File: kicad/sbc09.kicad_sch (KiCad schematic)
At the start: 82 parts, among them J1 Conn_01x04_Male, J2 Conn_01x06_Male, J3 Conn_01x06_Male, J4 Conn_01x06_Male, J5 Conn_02x05_Odd_Even, J6 Conn_02x25_Odd_Even, J7 Conn_02x05_Odd_Even, Q1 2N7000, SW1 SW_Push, U1 74HCT245, U10 SST39SF040-DIP, U11 XR68C681CJ, U12 MAX232, U2 74HCT245, U3 74HCT245, U4 MC6809E, U5 74HCT32, U6 EPM7128SLC84, U7 71256SA15TPG, U8 AS6C4008-55PCN, U9 SST39SF040-DIP, X1 8MHz, X2 3.6864MHz

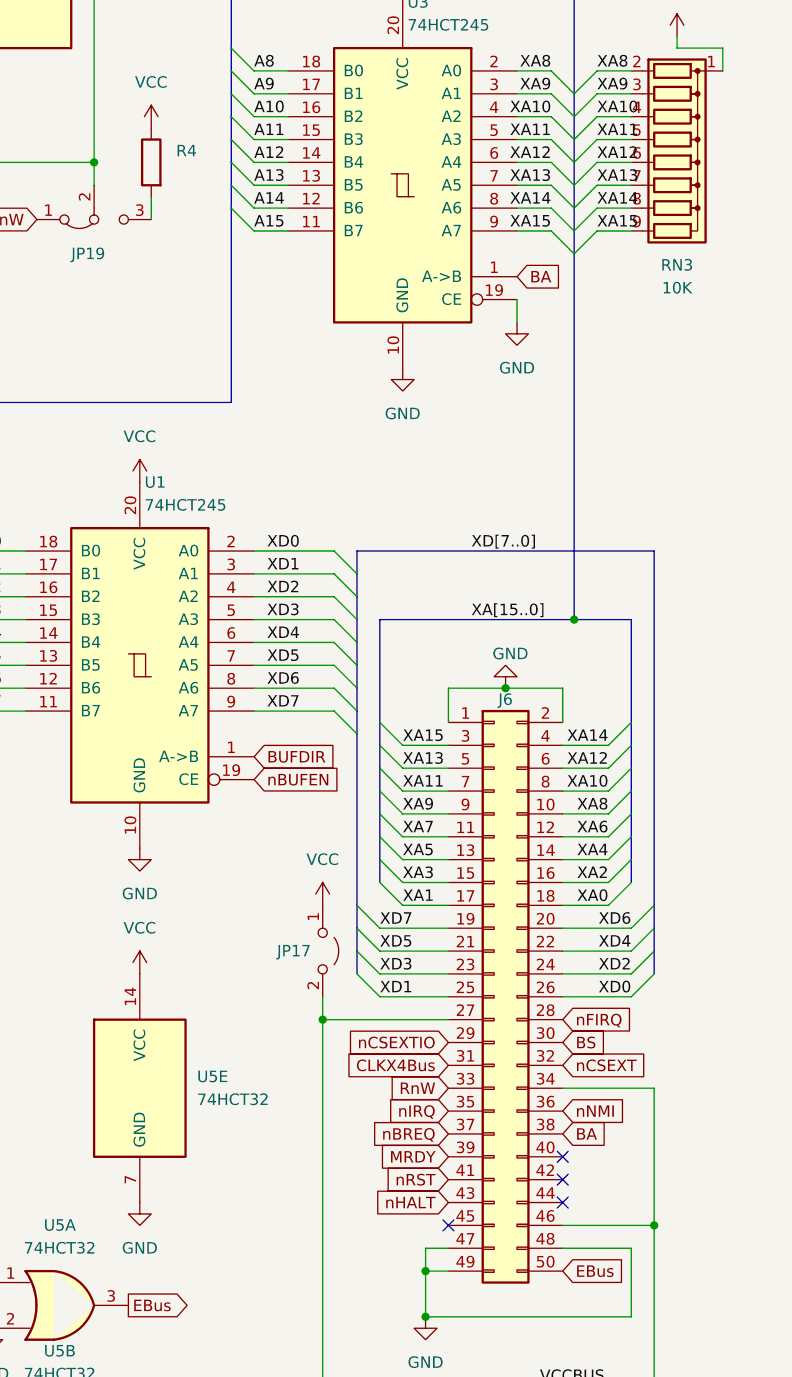
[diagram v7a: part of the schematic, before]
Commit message: KiCAD: Connect QA13/14/15 to spare pins on the backplane connector (review assignments)
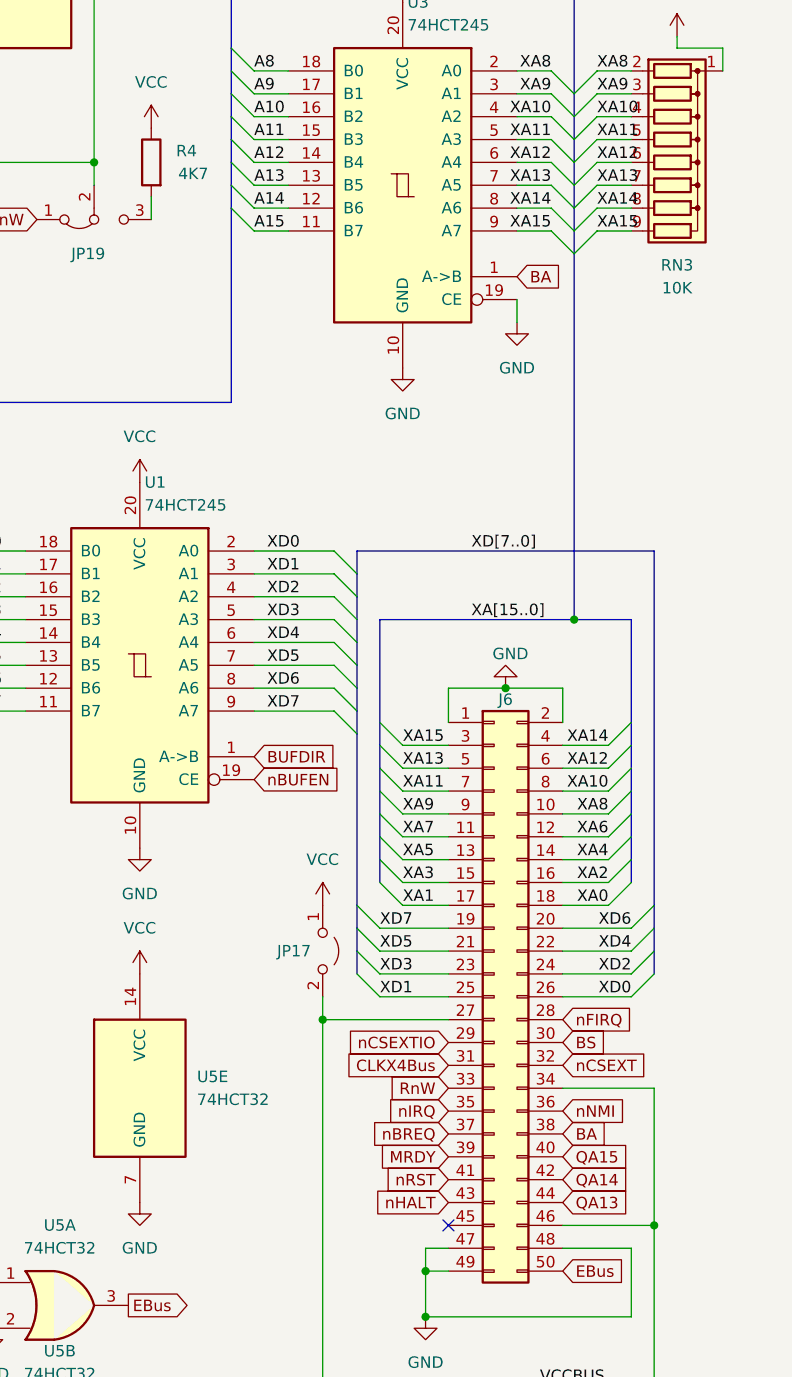
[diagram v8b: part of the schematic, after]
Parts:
- R4: value (none) -> 4K7
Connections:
- net QA13: now also J6.44 (Pin_44)
- net QA14: now also J6.42 (Pin_42)
- net QA15: now also J6.40 (Pin_40)
- no-connect marks 24 -> 21
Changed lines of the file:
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@@
   (no_connect (at 105.41 171.45))
   (no_connect (at 217.17 162.56))
-  (no_connect (at 389.89 214.63))
   (no_connect (at 17.145 202.565))
   (no_connect (at 313.69 210.82))
   (no_connect (at 218.948 262.382))
   (no_connect (at 217.17 190.5))
-  (no_connect (at 389.89 212.09))
   (no_connect (at 180.34 203.2))
-  (no_connect (at 389.89 217.17))
   (no_connect (at 300.99 200.66))
   (no_connect (at 300.99 208.28))
@@
     )
   )
+  (global_label "QA15" (shape input) (at 389.89 212.09 0) (fields_autoplaced)
+    (effects (font (size 1.27 1.27)) (justify left))
+    (property "Intersheet References" "${INTERSHEET_REFS}" (id 0) (at 397.1412 212.0106 0)
+      (effects (font (size 1.27 1.27)) (justify left) hide)
+    )
+  )
   (global_label "nCSUART" (shape input) (at 125.73 218.44 180) (fields_autoplaced)
     (effects (font (size 1.27 1.27)) (justify right))
@@
     )
   )
+  (global_label "QA14" (shape input) (at 389.89 214.63 0) (fields_autoplaced)
+    (effects (font (size 1.27 1.27)) (justify left))
+    (property "Intersheet References" "${INTERSHEET_REFS}" (id 0) (at 397.1412 214.5506 0)
+      (effects (font (size 1.27 1.27)) (justify left) hide)
+    )
+  )
   (global_label "nNMI" (shape input) (at 389.89 207.01 0) (fields_autoplaced)
     (effects (font (size 1.27 1.27)) (justify left))
@@
     )
   )
+  (global_label "QA13" (shape input) (at 389.89 217.17 0) (fields_autoplaced)
+    (effects (font (size 1.27 1.27)) (justify left))
+    (property "Intersheet References" "${INTERSHEET_REFS}" (id 0) (at 397.1412 217.0906 0)
+      (effects (font (size 1.27 1.27)) (justify left) hide)
+    )
+  )
   (global_label "SDCS" (shape input) (at 163.83 147.32 180) (fields_autoplaced)
     (effects (font (size 1.27 1.27)) (justify right))
@@
       (effects (font (size 1.27 1.27)) (justify left))
     )
-    (property "Value" "" (id 1) (at 350.52 102.87 0)
+    (property "Value" "4K7" (id 1) (at 350.52 102.87 0)
       (effects (font (size 1.27 1.27)) (justify left))
     )
